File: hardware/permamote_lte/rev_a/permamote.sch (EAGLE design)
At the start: 118 parts, among them IC1 NRF9160, J1 TC2030-JLINK-NL, J2 U.FL-R-SMT, J3 NANO_SIM, J4 U.FL-R-SMT, J5 DM3AT-SF-PEJM5, Q1 PMDXB950UPEL, Q10 PMDXB950UPEL, Q2 PMDXB950UPEL, Q3 PMDXB950UPEL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

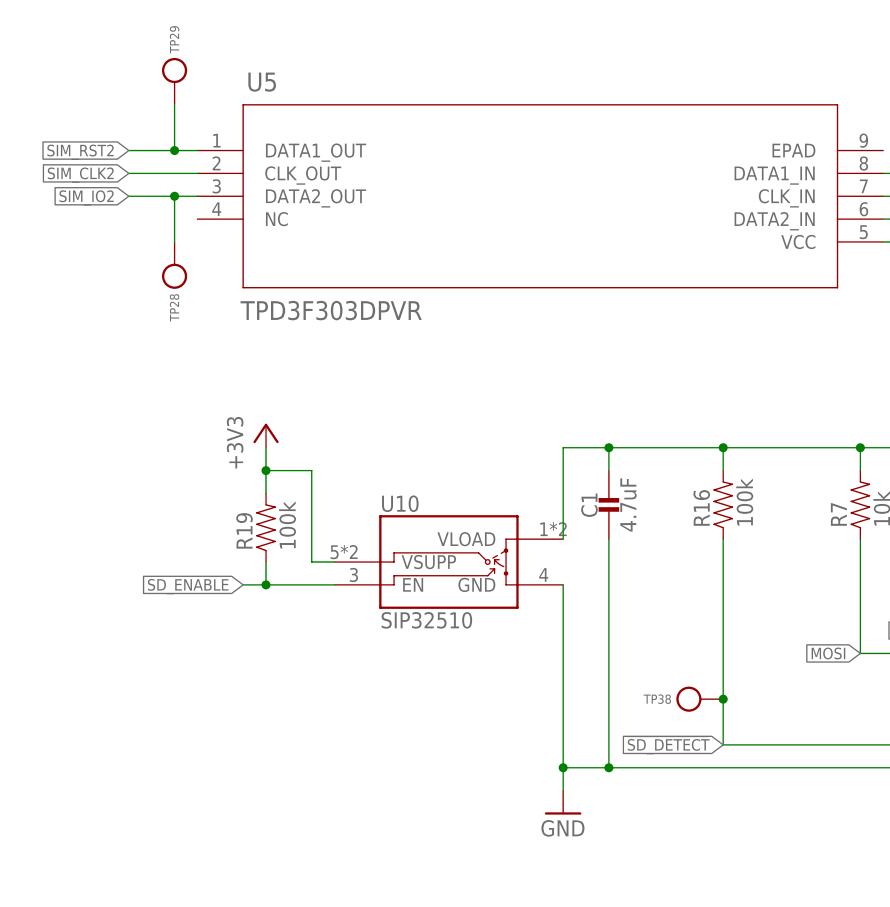
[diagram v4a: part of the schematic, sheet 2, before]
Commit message: routed everything except confused about ground and vcc
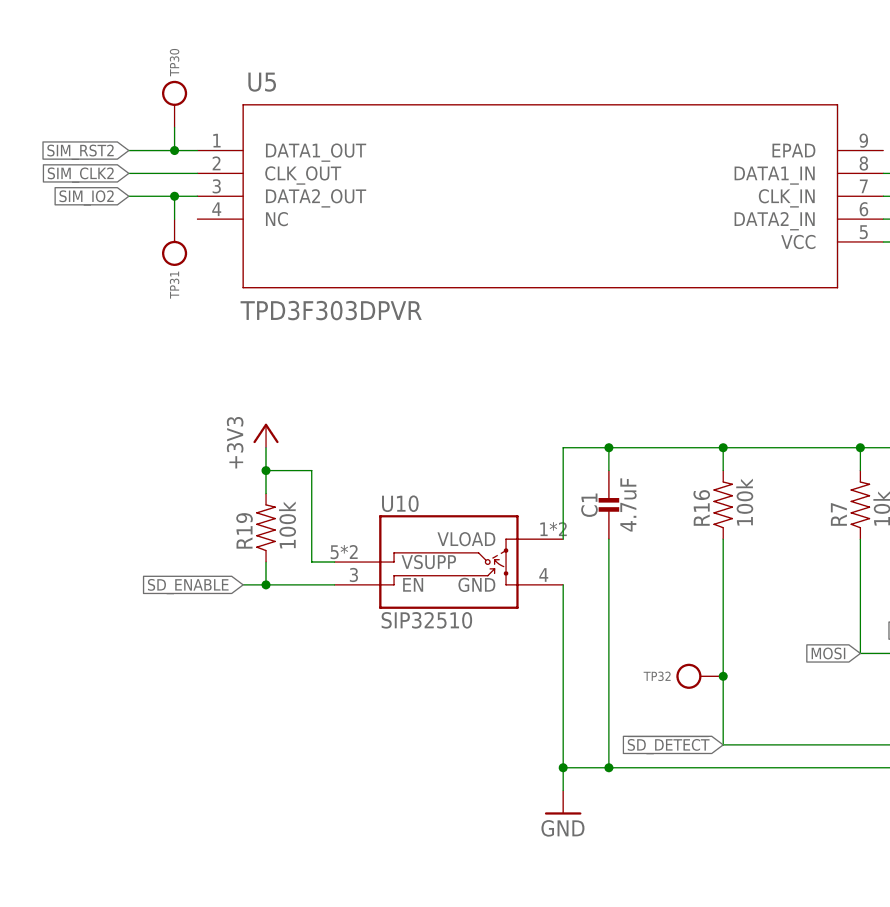
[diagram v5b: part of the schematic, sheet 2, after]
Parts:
- removed TP28, TP29, TP38: TEST_POINT_0.040IN, headers:TEST_POINT_0.040IN
- added TP30, TP31, TP32: TEST-POINT, headers:TEST-POINT
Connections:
- net !SD_DETECT: now also TP32.TESTPOINT; no longer TP38.TESTPOINT
- net MISO: now also IC1.P0.22; no longer IC1.P0.21
- net MOSI: now also IC1.P0.21; no longer IC1.P0.22
- net SIM_IO2: now also TP31.TESTPOINT; no longer TP28.TESTPOINT
- net SIM_RST2: now also TP30.TESTPOINT; no longer TP29.TESTPOINT
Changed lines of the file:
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@@
 </part>
 <part name="+3V8" library="regulators" deviceset="+3V3" device=""/>
-<part name="TP38" library="headers" deviceset="TEST_POINT_0.040IN" device=""/>
 <part name="FRAME4" library="lab11-frames" deviceset="LETTER_L_BLANK" device="">
 <attribute name="REV" value="A"/>
 <attribute name="TITLE" value="PERMAMOTE_LTE"/>
 </part>
-<part name="TP28" library="headers" deviceset="TEST_POINT_0.040IN" device=""/>
-<part name="TP29" library="headers" deviceset="TEST_POINT_0.040IN" device=""/>
+<part name="TP30" library="headers" deviceset="TEST-POINT" device=""/>
+<part name="TP31" library="headers" deviceset="TEST-POINT" device=""/>
+<part name="TP32" library="headers" deviceset="TEST-POINT" device=""/>
 </parts>
 <sheets>
@@
 </segment>
 <segment>
+<label x="111.76" y="83.82" size="1.27" layer="95" rot="R270" xref="yes"/>
+<wire x1="111.76" y1="83.82" x2="111.76" y2="88.9" width="0.1524" layer="91"/>
+<pinref part="IC1" gate="G$1" pin="P0.22"/>
+</segment>
+</net>
+<net name="MOSI" class="0">
+<segment>
+<pinref part="U1" gate="G$1" pin="SDI"/>
+<wire x1="50.8" y1="17.78" x2="48.26" y2="17.78" width="0.1524" layer="91"/>
+<label x="48.26" y="17.78" size="1.27" layer="95" rot="R180" xref="yes"/>
+</segment>
+<segment>
 <label x="109.22" y="83.82" size="1.27" layer="95" rot="R270" xref="yes"/>
 <wire x1="109.22" y1="83.82" x2="109.22" y2="88.9" width="0.1524" layer="91"/>
 <pinref part="IC1" gate="G$1" pin="P0.21"/>
-</segment>
-</net>
-<net name="MOSI" class="0">
-<segment>
-<pinref part="U1" gate="G$1" pin="SDI"/>
-<wire x1="50.8" y1="17.78" x2="48.26" y2="17.78" width="0.1524" layer="91"/>
-<label x="48.26" y="17.78" size="1.27" layer="95" rot="R180" xref="yes"/>
-</segment>
-<segment>
-<label x="111.76" y="83.82" size="1.27" layer="95" rot="R270" xref="yes"/>
-<wire x1="111.76" y1="83.82" x2="111.76" y2="88.9" width="0.1524" layer="91"/>
-<pinref part="IC1" gate="G$1" pin="P0.22"/>
 </segment>
 </net>
@@
 <attribute name="VALUE" x="58.42" y="83.82" size="1.778" layer="96" rot="R90"/>
 </instance>
-<instance part="TP38" gate="G$1" x="109.22" y="58.42" smashed="yes">
-<attribute name="NAME" x="106.045" y="58.42" size="1.016" layer="95" ratio="12" align="center-right"/>
-</instance>
 <instance part="FRAME4" gate="G$1" x="0" y="0" smashed="yes"/>
 <instance part="FRAME4" gate="G$2" x="152.4" y="0" smashed="yes">
@@
 <attribute name="AUTHOR" x="169.545" y="6.35" size="2.54" layer="94" font="vector"/>
 </instance>
-<instance part="TP28" gate="G$1" x="50.8" y="106.68" smashed="yes" rot="R90">
-<attribute name="NAME" x="50.8" y="103.505" size="1.016" layer="95" ratio="12" rot="R90" align="center-right"/>
-</instance>
-<instance part="TP29" gate="G$1" x="50.8" y="127" smashed="yes" rot="R270">
-<attribute name="NAME" x="50.8" y="130.175" size="1.016" layer="95" ratio="12" rot="R270" align="center-right"/>
+<instance part="TP30" gate="G$1" x="50.8" y="124.46" smashed="yes" rot="R270">
+<attribute name="NAME" x="50.8" y="127.635" size="1.016" layer="95" ratio="12" rot="R270" align="center-right"/>
+</instance>
+<instance part="TP31" gate="G$1" x="50.8" y="109.22" smashed="yes" rot="R90">
+<attribute name="NAME" x="50.8" y="106.045" size="1.016" layer="95" ratio="12" rot="R90" align="center-right"/>
+</instance>
+<instance part="TP32" gate="G$1" x="109.22" y="60.96" smashed="yes">
+<attribute name="NAME" x="106.045" y="60.96" size="1.016" layer="95" ratio="12" align="center-right"/>
 </instance>
 </instances>
@@
 <wire x1="53.34" y1="119.38" x2="50.8" y2="119.38" width="0.1524" layer="91"/>
 <label x="45.72" y="119.38" size="1.27" layer="95" rot="R180" xref="yes"/>
-<pinref part="TP29" gate="G$1" pin="TESTPOINT"/>
 <wire x1="50.8" y1="119.38" x2="45.72" y2="119.38" width="0.1524" layer="91"/>
-<wire x1="50.8" y1="124.46" x2="50.8" y2="119.38" width="0.1524" layer="91"/>
+<wire x1="50.8" y1="121.92" x2="50.8" y2="119.38" width="0.1524" layer="91"/>
 <junction x="50.8" y="119.38"/>
+<pinref part="TP30" gate="G$1" pin="TESTPOINT"/>
 </segment>
 <segment>
@@
 <wire x1="53.34" y1="114.3" x2="50.8" y2="114.3" width="0.1524" layer="91"/>
 <label x="45.72" y="114.3" size="1.27" layer="95" rot="R180" xref="yes"/>
-<pinref part="TP28" gate="G$1" pin="TESTPOINT"/>
 <wire x1="50.8" y1="114.3" x2="45.72" y2="114.3" width="0.1524" layer="91"/>
-<wire x1="50.8" y1="114.3" x2="50.8" y2="109.22" width="0.1524" layer="91"/>
+<wire x1="50.8" y1="114.3" x2="50.8" y2="111.76" width="0.1524" layer="91"/>
 <junction x="50.8" y="114.3"/>
+<pinref part="TP31" gate="G$1" pin="TESTPOINT"/>
 </segment>
 <segment>
@@
 <pinref part="R16" gate="G$1" pin="1"/>
 <wire x1="157.48" y1="53.34" x2="111.76" y2="53.34" width="0.1524" layer="91"/>
-<wire x1="111.76" y1="53.34" x2="111.76" y2="58.42" width="0.1524" layer="91"/>
+<wire x1="111.76" y1="53.34" x2="111.76" y2="60.96" width="0.1524" layer="91"/>
 <label x="111.76" y="53.34" size="1.27" layer="95" font="vector" rot="R180" xref="yes"/>
-<pinref part="TP38" gate="G$1" pin="TESTPOINT"/>
-<wire x1="111.76" y1="58.42" x2="111.76" y2="76.2" width="0.1524" layer="91"/>
-<junction x="111.76" y="58.42"/>
-</segment>
-</net>
+<pinref part="TP32" gate="G$1" pin="TESTPOINT"/>
+<wire x1="111.76" y1="60.96" x2="111.76" y2="76.2" width="0.1524" layer="91"/>
+<junction x="111.76" y="60.96"/>
+</segment>
+</net>

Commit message: more routing fixes
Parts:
- removed C33, C34: DNP, passives:CAPACITOR0402_CAP
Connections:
- removed net N$26: C33.1, U1.XI, X4.1
- removed net N$27: C34.1, U1.XO, X4.2
- net GND: now also U1.XI, U1.XO, X4.1, X4.2; no longer C33.2, C34.2
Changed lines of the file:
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@@
 <part name="GND14" library="supply1" library_urn="urn:adsk.eagle:library:371" deviceset="GND" device=""/>
 <part name="X4" library="crystals" deviceset="ABS07-32.768KHZ" device="-7-T" value="ABS07-32.768KHZ-7-T"/>
-<part name="C33" library="passives" deviceset="CAPACITOR" device="0402_CAP" value="DNP"/>
-<part name="C34" library="passives" deviceset="CAPACITOR" device="0402_CAP" value="DNP"/>
 <part name="C26" library="passives" deviceset="CAPACITOR" device="0402_CAP" value="1uF">
 <attribute name="DIGIKEY" value="490-7195-1-ND "/>
@@
 <attribute name="VALUE" x="15.24" y="35.56" size="1.27" layer="96"/>
 </instance>
-<instance part="C33" gate="G$1" x="12.7" y="22.86" smashed="yes">
-<attribute name="NAME" x="11.43" y="21.59" size="1.778" layer="95" ratio="12" rot="R90" align="bottom-center"/>
-<attribute name="VALUE" x="13.97" y="21.59" size="1.778" layer="96" ratio="12" rot="R270" align="bottom-center"/>
-</instance>
-<instance part="C34" gate="G$1" x="22.86" y="22.86" smashed="yes">
-<attribute name="NAME" x="21.59" y="21.59" size="1.778" layer="95" ratio="12" rot="R90" align="bottom-center"/>
-<attribute name="VALUE" x="24.13" y="21.59" size="1.778" layer="96" ratio="12" rot="R270" align="bottom-center"/>
-</instance>
 <instance part="C26" gate="G$1" x="7.62" y="38.1" smashed="yes">
 <attribute name="DIGIKEY" x="7.62" y="38.1" size="1.778" layer="96" display="off"/>
@@
 <wire x1="7.62" y1="15.24" x2="12.7" y2="15.24" width="0.1524" layer="91"/>
 <junction x="30.48" y="15.24"/>
-<pinref part="C33" gate="G$1" pin="2"/>
 <wire x1="12.7" y1="15.24" x2="22.86" y2="15.24" width="0.1524" layer="91"/>
 <wire x1="22.86" y1="15.24" x2="30.48" y2="15.24" width="0.1524" layer="91"/>
-<wire x1="12.7" y1="17.78" x2="12.7" y2="15.24" width="0.1524" layer="91"/>
 <junction x="12.7" y="15.24"/>
-<pinref part="C34" gate="G$1" pin="2"/>
-<wire x1="22.86" y1="17.78" x2="22.86" y2="15.24" width="0.1524" layer="91"/>
 <junction x="22.86" y="15.24"/>
 <pinref part="C26" gate="G$1" pin="2"/>
+<pinref part="X4" gate="G$1" pin="1"/>
+<wire x1="12.7" y1="30.48" x2="12.7" y2="40.64" width="0.1524" layer="91"/>
+<junction x="12.7" y="30.48"/>
+<wire x1="12.7" y1="40.64" x2="35.56" y2="40.64" width="0.1524" layer="91"/>
+<wire x1="35.56" y1="40.64" x2="35.56" y2="35.56" width="0.1524" layer="91"/>
+<pinref part="U1" gate="G$1" pin="XI"/>
+<wire x1="35.56" y1="35.56" x2="50.8" y2="35.56" width="0.1524" layer="91"/>
+<wire x1="12.7" y1="30.48" x2="12.7" y2="15.24" width="0.1524" layer="91"/>
+<pinref part="X4" gate="G$1" pin="2"/>
+<pinref part="U1" gate="G$1" pin="XO"/>
+<wire x1="50.8" y1="33.02" x2="22.86" y2="33.02" width="0.1524" layer="91"/>
+<wire x1="22.86" y1="33.02" x2="22.86" y2="30.48" width="0.1524" layer="91"/>
+<junction x="22.86" y="30.48"/>
+<wire x1="22.86" y1="30.48" x2="22.86" y2="15.24" width="0.1524" layer="91"/>
 </segment>
 <segment>
@@
 </segment>
 </net>
-<net name="N$26" class="0">
-<segment>
-<pinref part="X4" gate="G$1" pin="1"/>
-<pinref part="C33" gate="G$1" pin="1"/>
-<wire x1="12.7" y1="30.48" x2="12.7" y2="25.4" width="0.1524" layer="91"/>
-<wire x1="12.7" y1="30.48" x2="12.7" y2="40.64" width="0.1524" layer="91"/>
-<junction x="12.7" y="30.48"/>
-<wire x1="12.7" y1="40.64" x2="35.56" y2="40.64" width="0.1524" layer="91"/>
-<wire x1="35.56" y1="40.64" x2="35.56" y2="35.56" width="0.1524" layer="91"/>
-<pinref part="U1" gate="G$1" pin="XI"/>
-<wire x1="35.56" y1="35.56" x2="50.8" y2="35.56" width="0.1524" layer="91"/>
-</segment>
-</net>
-<net name="N$27" class="0">
-<segment>
-<pinref part="X4" gate="G$1" pin="2"/>
-<pinref part="C34" gate="G$1" pin="1"/>
-<wire x1="22.86" y1="30.48" x2="22.86" y2="25.4" width="0.1524" layer="91"/>
-<pinref part="U1" gate="G$1" pin="XO"/>
-<wire x1="50.8" y1="33.02" x2="22.86" y2="33.02" width="0.1524" layer="91"/>
-<wire x1="22.86" y1="33.02" x2="22.86" y2="30.48" width="0.1524" layer="91"/>
-<junction x="22.86" y="30.48"/>
-</segment>
-</net>
